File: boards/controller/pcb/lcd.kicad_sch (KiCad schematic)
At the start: 5 parts, among them J10001 LCD

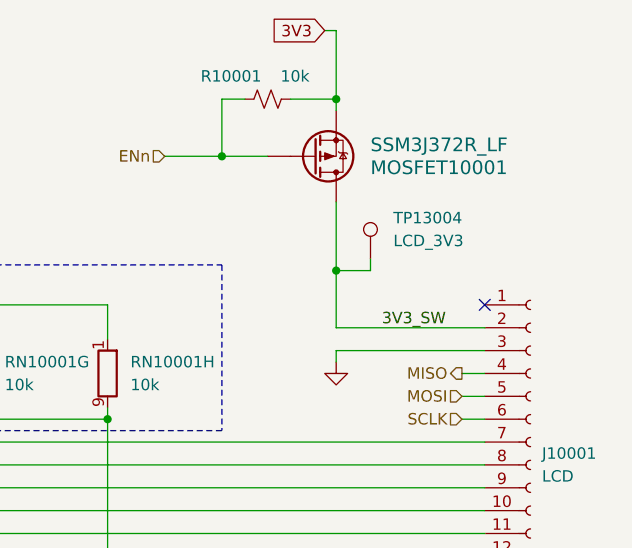
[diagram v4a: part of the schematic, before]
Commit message: controller: pcb: Update schematic + layout
Signed-off-by: Nicholas Loehrke <nicholasnloehrke@gmail.com>
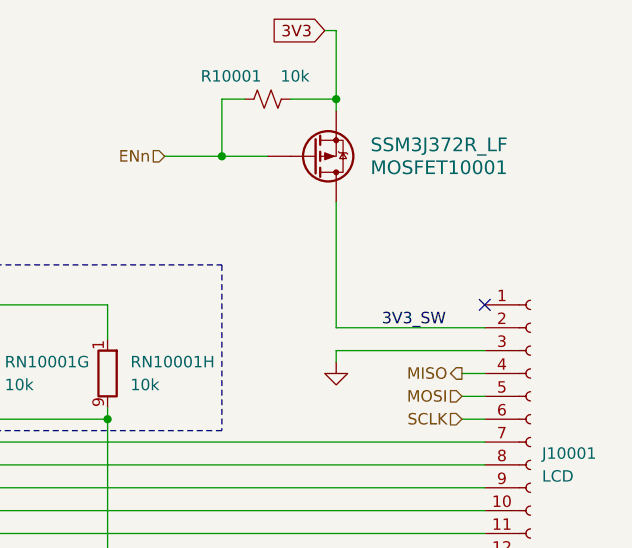
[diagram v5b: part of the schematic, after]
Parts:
- removed TP13004: LCD_3V3, symbol Connector:TestPoint
- MOSFET10001: footprint SOT-23F_TOS -> SSM3J372R_LF:SSM3J372R_LF
- R10001: footprint (none) -> Resistor_SMD:R_0402_1005Metric
- RN10001: footprint Resistor_THT:R_Array_SIP9 -> YC248-JR-0710KL:YC248-JR-0710KL
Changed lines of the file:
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@@
-	)
-	(junction
-		(at 209.55 85.09)
-		(diameter 0)
-		(color 0 0 0 0)
 	)
 	(junction
@@
 	(wire
 		(pts
-			(xy 213.36 83.82) (xy 213.36 85.09)
-		)
-		(stroke
-			(width 0)
-			(type default)
-		)
-	)
-	(wire
-		(pts
 			(xy 87.63 88.9) (xy 87.63 92.71)
 		)
@@
 	(wire
 		(pts
-			(xy 209.55 91.44) (xy 209.55 85.09)
+			(xy 209.55 77.47) (xy 209.55 91.44)
 		)
 		(stroke
@@
 	(wire
 		(pts
-			(xy 209.55 85.09) (xy 213.36 85.09)
-		)
-		(stroke
-			(width 0)
-			(type default)
-		)
-	)
-	(wire
-		(pts
 			(xy 101.6 88.9) (xy 115.57 88.9)
 		)
@@
 		(stroke
 			(width 0)
-			(type default)
-		)
-	)
-	(wire
-		(pts
-			(xy 209.55 85.09) (xy 209.55 77.47)
-		)
-		(stroke
-			(width 0.508)
 			(type default)
 		)
@@
 			)
 		)
-		(property "Footprint" "Resistor_THT:R_Array_SIP9"
+		(property "Footprint" "YC248-JR-0710KL:YC248-JR-0710KL"
 			(at 151.638 96.52 90)
 			(effects
@@
 			)
 		)
-		(property "Footprint" "Resistor_THT:R_Array_SIP9"
+		(property "Footprint" "YC248-JR-0710KL:YC248-JR-0710KL"
 			(at 113.538 96.52 90)
 			(effects
@@
 					(reference "RN10001")
 					(unit 4)
-				)
-			)
-		)
-	)
-	(symbol
-		(lib_id "Connector:TestPoint")
-		(at 213.36 83.82 0)
-		(unit 1)
-		(exclude_from_sim no)
-		(in_bom yes)
-		(on_board yes)
-		(dnp no)
-		(fields_autoplaced yes)
-		(property "Reference" "TP13004"
-			(at 215.9 79.2479 0)
-			(effects
-				(font
-					(size 1.27 1.27)
-				)
-				(justify left)
-			)
-		)
-		(property "Value" "LCD_3V3"
-			(at 215.9 81.7879 0)
-			(effects
-				(font
-					(size 1.27 1.27)
-				)
-				(justify left)
-			)
-		)
-		(property "Footprint" ""
-			(at 218.44 83.82 0)
-			(effects
-				(font
-					(size 1.27 1.27)
-				)
-				(hide yes)
-			)
-		)
-		(property "Datasheet" "~"
-			(at 218.44 83.82 0)
-			(effects
-				(font
-					(size 1.27 1.27)
-				)
-				(hide yes)
-			)
-		)
-		(property "Description" "test point"
-			(at 213.36 83.82 0)
-			(effects
-				(font
-					(size 1.27 1.27)
-				)
-				(hide yes)
-			)
-		)
-		(pin "1"
-		)
-		(instances
-			(project "controller"
-				(path "/5caba13a-97ae-46d4-856f-900b12012fd8/397b981f-9e39-4a0b-88ba-1021bd78e3f7"
-					(reference "TP13004")
-					(unit 1)
 				)
 			)
@@
 			)
 		)
-		(property "Footprint" "Resistor_THT:R_Array_SIP9"
+		(property "Footprint" "YC248-JR-0710KL:YC248-JR-0710KL"
 			(at 137.668 96.52 90)
 			(effects
@@
 			)
 		)
-		(property "Footprint" "Resistor_THT:R_Array_SIP9"
+		(property "Footprint" "YC248-JR-0710KL:YC248-JR-0710KL"
 			(at 182.118 96.52 90)
 			(effects
@@
 			)
 		)
-		(property "Footprint" "Resistor_THT:R_Array_SIP9"
+		(property "Footprint" "YC248-JR-0710KL:YC248-JR-0710KL"
 			(at 99.568 96.52 90)
 			(effects
@@
 			)
 		)
-		(property "Footprint" "Resistor_THT:R_Array_SIP9"
+		(property "Footprint" "YC248-JR-0710KL:YC248-JR-0710KL"
 			(at 168.148 96.52 90)
 			(effects
@@
 			)
 		)
-		(property "Footprint" "Resistor_THT:R_Array_SIP9"
+		(property "Footprint" "YC248-JR-0710KL:YC248-JR-0710KL"
 			(at 71.628 96.52 90)
 			(effects
@@
 			)
 		)
-		(property "Footprint" "Resistor_THT:R_Array_SIP9"
+		(property "Footprint" "YC248-JR-0710KL:YC248-JR-0710KL"
 			(at 85.598 96.52 90)
 			(effects
@@
 			)
 		)
-		(property "Footprint" ""
+		(property "Footprint" "Resistor_SMD:R_0402_1005Metric"
 			(at 201.93 66.04 0)
 			(effects
@@
 			)
 		)
-		(property "Footprint" "SOT-23F_TOS"
+		(property "Footprint" "SSM3J372R_LF:SSM3J372R_LF"
 			(at 199.898 81.534 0)
 			(effects

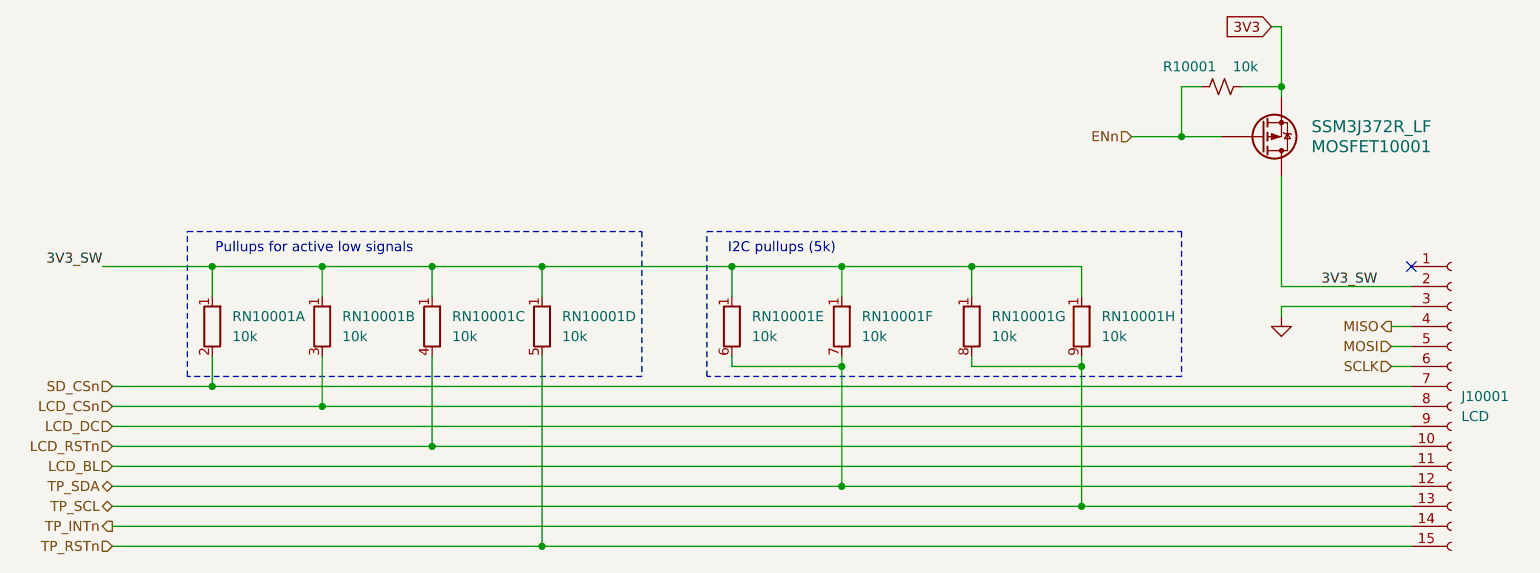
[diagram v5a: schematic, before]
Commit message: controller: Update BOM
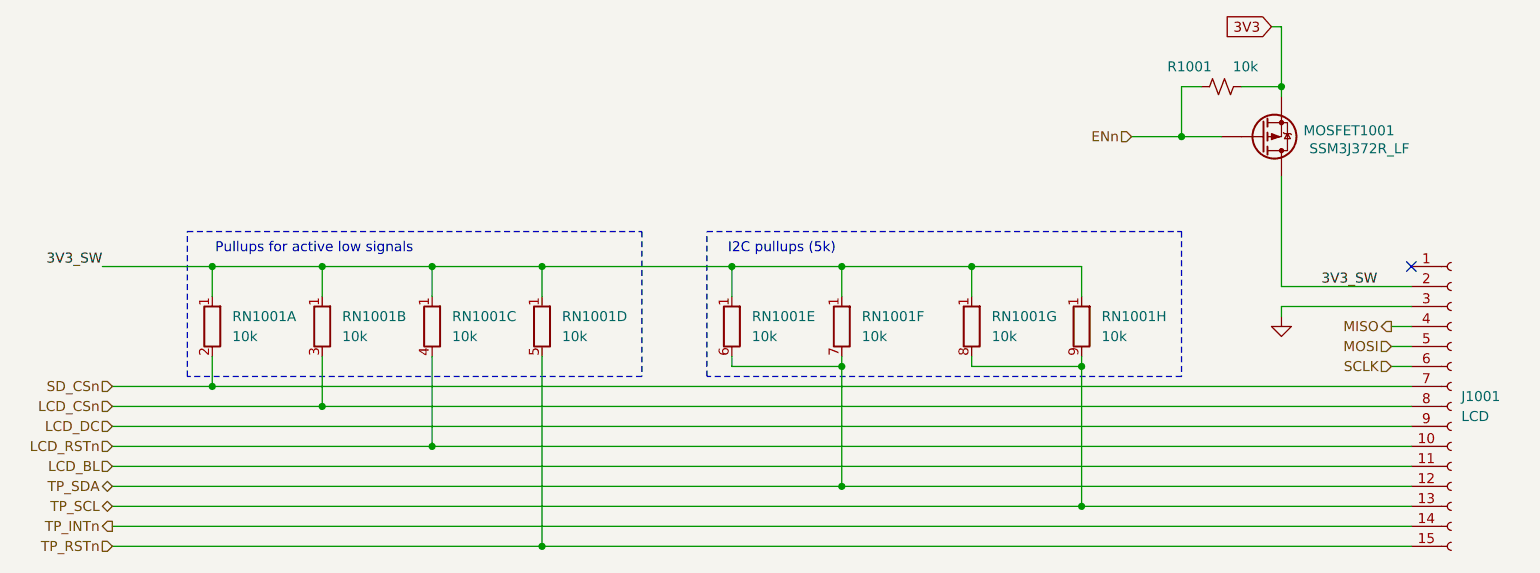
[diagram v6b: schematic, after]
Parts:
- MOSFET1001: renamed from MOSFET10001; MPN (none) -> SSM3J372R_LF
- RN1001: renamed from RN10001; MPN (none) -> YC248-JR-0710KL
- renumbered J10001 to J1001, R10001 to R1001
